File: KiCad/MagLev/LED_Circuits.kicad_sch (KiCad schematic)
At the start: 51 parts, among them Q1 ZX5T851GTA

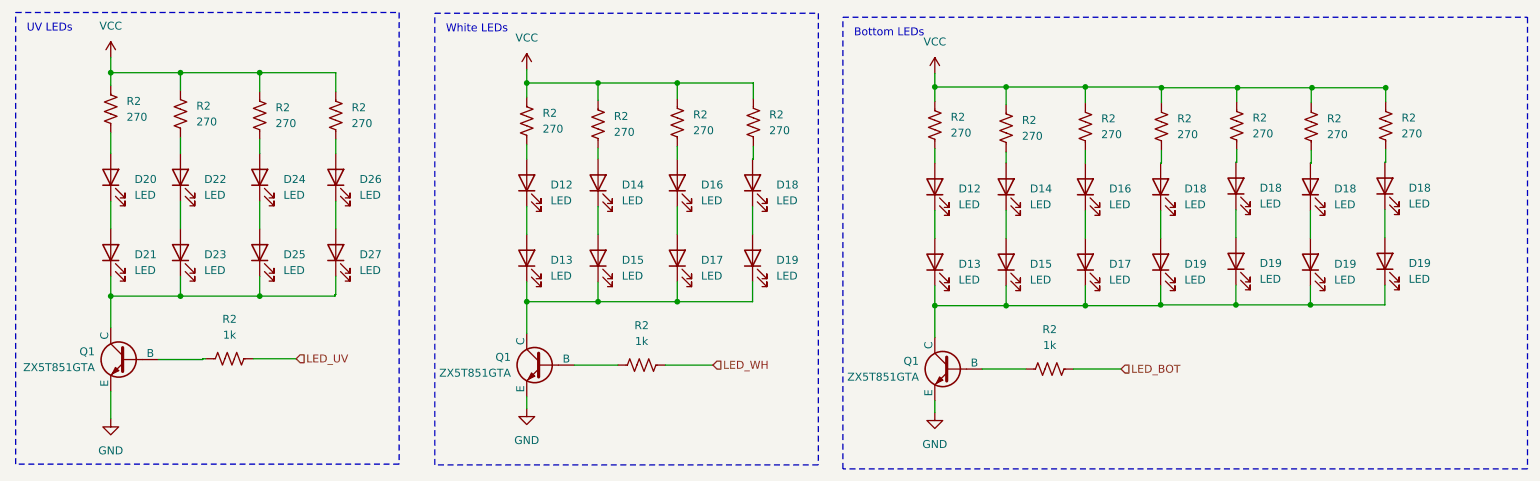
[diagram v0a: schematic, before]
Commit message: Update LED PCB reference after adding new LED schematic sheet.
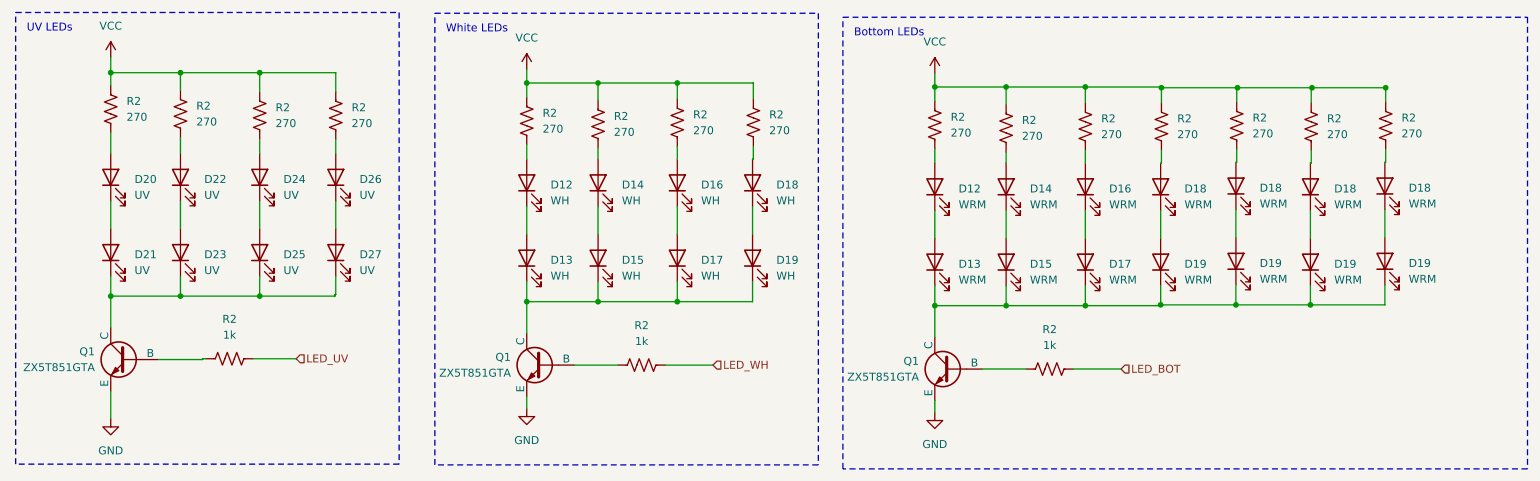
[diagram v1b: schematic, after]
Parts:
- D12, D13, D14, D15, D16, D17, D18, D19: value LED -> WH; PN (none) -> LTW-170TK; Part LTW-170TK -> (none)
- D12, D13, D14, D15, D16, D17, D18, D19: value LED -> WRM; PN (none) -> LTW-170TK; Part LTW-170TK -> (none)
- D20: value LED -> UV; PN (none) -> ATS2012UV415; Part: ATS2012UV415 -> (none)
- D21, D22, D23, D24, D25, D26, D27: value LED -> UV; PN (none) -> ATS2012UV415; Part ATS2012UV415 -> (none)
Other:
- company: (none) -> Kevin Dueck
- title: (none) -> LED Circuit

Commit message: Update BOM with JLCPCB PNs.
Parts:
- Q1: JLC Part Number (none) -> C99985
- R2: JLC Part Number (none) -> C17590
- R2: JLC Part Number (none) -> C17513
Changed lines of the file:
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@@
       (effects (font (size 1.27 1.27)) hide)
     )
-    (property "JLC Part Number" "" (at 81.28 79.883 0)
+    (property "JLC Part Number" "C17590" (at 81.28 79.883 0)
       (effects (font (size 1.27 1.27)) hide)
     )
@@
       (effects (font (size 1.27 1.27)) hide)
     )
-    (property "JLC Part Number" "" (at 225.679 81.534 0)
+    (property "JLC Part Number" "C17590" (at 225.679 81.534 0)
       (effects (font (size 1.27 1.27)) hide)
     )
@@
       (effects (font (size 1.27 1.27)) hide)
     )
-    (property "JLC Part Number" "" (at 45.212 78.867 0)
+    (property "JLC Part Number" "C17590" (at 45.212 78.867 0)
       (effects (font (size 1.27 1.27)) hide)
     )
@@
       (effects (font (size 1.27 1.27)) hide)
     )
-    (property "JLC Part Number" "" (at 47.752 118.999 0)
+    (property "JLC Part Number" "C99985" (at 47.752 118.999 0)
       (effects (font (size 1.27 1.27)) hide)
     )
@@
       (effects (font (size 1.27 1.27)) hide)
     )
-    (property "JLC Part Number" "" (at 237.617 81.661 0)
+    (property "JLC Part Number" "C17590" (at 237.617 81.661 0)
       (effects (font (size 1.27 1.27)) hide)
     )
@@
       (effects (font (size 1.27 1.27)) hide)
     )
-    (property "JLC Part Number" "" (at 130.302 119.888 0)
+    (property "JLC Part Number" "C17513" (at 130.302 119.888 0)
       (effects (font (size 1.27 1.27)) hide)
     )
@@
       (effects (font (size 1.27 1.27)) hide)
     )
-    (property "JLC Part Number" "" (at 69.088 79.883 0)
+    (property "JLC Part Number" "C17590" (at 69.088 79.883 0)
       (effects (font (size 1.27 1.27)) hide)
     )
@@
       (effects (font (size 1.27 1.27)) hide)
     )
-    (property "JLC Part Number" "" (at 188.722 81.915 0)
+    (property "JLC Part Number" "C17590" (at 188.722 81.915 0)
       (effects (font (size 1.27 1.27)) hide)
     )
@@
       (effects (font (size 1.27 1.27)) hide)
     )
-    (property "JLC Part Number" "" (at 213.614 81.661 0)
+    (property "JLC Part Number" "C17590" (at 213.614 81.661 0)
       (effects (font (size 1.27 1.27)) hide)
     )
@@
       (effects (font (size 1.27 1.27)) hide)
     )
-    (property "JLC Part Number" "" (at 195.707 120.523 0)
+    (property "JLC Part Number" "C17513" (at 195.707 120.523 0)
       (effects (font (size 1.27 1.27)) hide)
     )
@@
       (effects (font (size 1.27 1.27)) hide)
     )
-    (property "JLC Part Number" "" (at 177.292 81.407 0)
+    (property "JLC Part Number" "C17590" (at 177.292 81.407 0)
       (effects (font (size 1.27 1.27)) hide)
     )
@@
       (effects (font (size 1.27 1.27)) hide)
     )
-    (property "JLC Part Number" "" (at 201.422 81.661 0)
+    (property "JLC Part Number" "C17590" (at 201.422 81.661 0)
       (effects (font (size 1.27 1.27)) hide)
     )
@@
       (effects (font (size 1.27 1.27)) hide)
     )
-    (property "JLC Part Number" "" (at 179.832 120.523 0)
+    (property "JLC Part Number" "C99985" (at 179.832 120.523 0)
       (effects (font (size 1.27 1.27)) hide)
     )
@@
       (effects (font (size 1.27 1.27)) hide)
     )
-    (property "JLC Part Number" "" (at 249.555 81.534 0)
+    (property "JLC Part Number" "C17590" (at 249.555 81.534 0)
       (effects (font (size 1.27 1.27)) hide)
     )
@@
       (effects (font (size 1.27 1.27)) hide)
     )
-    (property "JLC Part Number" "" (at 56.388 79.629 0)
+    (property "JLC Part Number" "C17590" (at 56.388 79.629 0)
       (effects (font (size 1.27 1.27)) hide)
     )
@@
       (effects (font (size 1.27 1.27)) hide)
     )
-    (property "JLC Part Number" "" (at 64.262 118.872 0)
+    (property "JLC Part Number" "C17513" (at 64.262 118.872 0)
       (effects (font (size 1.27 1.27)) hide)
     )
@@
       (effects (font (size 1.27 1.27)) hide)
     )
-    (property "JLC Part Number" "" (at 114.427 119.888 0)
+    (property "JLC Part Number" "C99985" (at 114.427 119.888 0)
       (effects (font (size 1.27 1.27)) hide)
     )
@@
       (effects (font (size 1.27 1.27)) hide)
     )
-    (property "JLC Part Number" "" (at 111.887 80.772 0)
+    (property "JLC Part Number" "C17590" (at 111.887 80.772 0)
       (effects (font (size 1.27 1.27)) hide)
     )
@@
       (effects (font (size 1.27 1.27)) hide)
     )
-    (property "JLC Part Number" "" (at 123.317 81.28 0)
+    (property "JLC Part Number" "C17590" (at 123.317 81.28 0)
       (effects (font (size 1.27 1.27)) hide)
     )
@@
       (effects (font (size 1.27 1.27)) hide)
     )
-    (property "JLC Part Number" "" (at 136.017 81.026 0)
+    (property "JLC Part Number" "C17590" (at 136.017 81.026 0)
       (effects (font (size 1.27 1.27)) hide)
     )
@@
       (effects (font (size 1.27 1.27)) hide)
     )
-    (property "JLC Part Number" "" (at 148.209 81.026 0)
-      (effects (font (size 1.27 1.27)) hide)
-    )
+    (property "JLC Part Number" "C17590" (at 148.209 81.026 0)
+      (effects (font (size 1.27 1.27)) hide)
+    )
